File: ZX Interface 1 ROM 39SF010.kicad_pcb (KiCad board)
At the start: 2 copper layers, 24.5 x 32 mm, 14 parts, among them J2 Conn_01x09_Pin, J4 BBL-112-G-E, SW1 SW_SPDT, U1 SST39SF040A TSOP

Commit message: Add files via upload
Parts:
- renumbered J2 to J1
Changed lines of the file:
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@@
   (net 22 "/A9")
   (net 23 "/A8")
-  (net 24 "Net-(J2-Pin_1)")
-  (net 25 "Net-(J2-Pin_2)")
-  (net 26 "Net-(J2-Pin_3)")
-  (net 27 "Net-(J2-Pin_4)")
-  (net 28 "Net-(J2-Pin_5)")
-  (net 29 "Net-(J2-Pin_6)")
-  (net 30 "Net-(J2-Pin_7)")
-  (net 31 "Net-(J2-Pin_8)")
+  (net 24 "Net-(J1-Pin_1)")
+  (net 25 "Net-(J1-Pin_2)")
+  (net 26 "Net-(J1-Pin_3)")
+  (net 27 "Net-(J1-Pin_4)")
+  (net 28 "Net-(J1-Pin_5)")
+  (net 29 "Net-(J1-Pin_6)")
+  (net 30 "Net-(J1-Pin_7)")
+  (net 31 "Net-(J1-Pin_8)")
   (net 32 "Net-(R2-Pad2)")
   (net 33 "/A4")
@@
       (net 23 "/A8") (pinfunction "A8") (pintype "input"))
     (pad "4" smd roundrect locked (at -6.6875 -2.25 270) (size 1.575 0.3) (layers "F.Cu" "F.Paste" "F.Mask") (roundrect_rratio 0.25)
-      (net 30 "Net-(J2-Pin_7)") (pinfunction "A13") (pintype "input"))
+      (net 30 "Net-(J1-Pin_7)") (pinfunction "A13") (pintype "input"))
     (pad "5" smd roundrect locked (at -6.6875 -1.75 270) (size 1.575 0.3) (layers "F.Cu" "F.Paste" "F.Mask") (roundrect_rratio 0.25)
-      (net 29 "Net-(J2-Pin_6)") (pinfunction "A14") (pintype "input"))
+      (net 29 "Net-(J1-Pin_6)") (pinfunction "A14") (pintype "input"))
     (pad "6" smd roundrect locked (at -6.6875 -1.25 270) (size 1.575 0.3) (layers "F.Cu" "F.Paste" "F.Mask") (roundrect_rratio 0.25)
-      (net 26 "Net-(J2-Pin_3)") (pinfunction "A17") (pintype "input"))
+      (net 26 "Net-(J1-Pin_3)") (pinfunction "A17") (pintype "input"))
     (pad "7" smd roundrect locked (at -6.6875 -0.75 270) (size 1.575 0.3) (layers "F.Cu" "F.Paste" "F.Mask") (roundrect_rratio 0.25)
-      (net 24 "Net-(J2-Pin_1)") (pinfunction "WE") (pintype "input"))
+      (net 24 "Net-(J1-Pin_1)") (pinfunction "WE") (pintype "input"))
     (pad "8" smd roundrect locked (at -6.6875 -0.25 270) (size 1.575 0.3) (layers "F.Cu" "F.Paste" "F.Mask") (roundrect_rratio 0.25)
       (net 1 "/VCC") (pinfunction "VCC") (pintype "power_in"))
     (pad "9" smd roundrect locked (at -6.6875 0.25 270) (size 1.575 0.3) (layers "F.Cu" "F.Paste" "F.Mask") (roundrect_rratio 0.25)
-      (net 25 "Net-(J2-Pin_2)") (pinfunction "A18") (pintype "input"))
+      (net 25 "Net-(J1-Pin_2)") (pinfunction "A18") (pintype "input"))
     (pad "10" smd roundrect locked (at -6.6875 0.75 270) (size 1.575 0.3) (layers "F.Cu" "F.Paste" "F.Mask") (roundrect_rratio 0.25)
-      (net 27 "Net-(J2-Pin_4)") (pinfunction "A16") (pintype "input"))
+      (net 27 "Net-(J1-Pin_4)") (pinfunction "A16") (pintype "input"))
     (pad "11" smd roundrect locked (at -6.6875 1.25 270) (size 1.575 0.3) (layers "F.Cu" "F.Paste" "F.Mask") (roundrect_rratio 0.25)
-      (net 28 "Net-(J2-Pin_5)") (pinfunction "A15") (pintype "input"))
+      (net 28 "Net-(J1-Pin_5)") (pinfunction "A15") (pintype "input"))
     (pad "12" smd roundrect locked (at -6.6875 1.75 270) (size 1.575 0.3) (layers "F.Cu" "F.Paste" "F.Mask") (roundrect_rratio 0.25)
       (net 21 "/A12") (pinfunction "A12") (pintype "input"))
@@
       (net 17 "/D7") (pinfunction "DQ7") (pintype "tri_state"))
     (pad "30" smd roundrect locked (at 6.6875 -2.75 270) (size 1.575 0.3) (layers "F.Cu" "F.Paste" "F.Mask") (roundrect_rratio 0.25)
-      (net 31 "Net-(J2-Pin_8)") (pinfunction "CE") (pintype "input"))
+      (net 31 "Net-(J1-Pin_8)") (pinfunction "CE") (pintype "input"))
     (pad "31" smd roundrect locked (at 6.6875 -3.25 270) (size 1.575 0.3) (layers "F.Cu" "F.Paste" "F.Mask") (roundrect_rratio 0.25)
       (net 19 "/A10") (pinfunction "A10") (pintype "input"))
@@
     (property "ki_keywords" "connector")
     (attr through_hole)
-    (fp_text reference "J2" (at 0 -2.77) (layer "F.SilkS")
+    (fp_text reference "J1" (at 0 -2.77) (layer "F.SilkS")
         (effects (font (size 1 1) (thickness 0.15)))
     )
@@
       (stroke (width 0.1) (type solid)) (layer "F.Fab"))
     (pad "1" thru_hole rect locked (at 0 0) (size 1.7 1.7) (drill 1) (layers "*.Cu" "*.Mask")
-      (net 24 "Net-(J2-Pin_1)") (pinfunction "Pin_1") (pintype "passive"))
+      (net 24 "Net-(J1-Pin_1)") (pinfunction "Pin_1") (pintype "passive"))
     (pad "2" thru_hole oval locked (at 0 2.54) (size 1.7 1.7) (drill 1) (layers "*.Cu" "*.Mask")
-      (net 25 "Net-(J2-Pin_2)") (pinfunction "Pin_2") (pintype "passive"))
+      (net 25 "Net-(J1-Pin_2)") (pinfunction "Pin_2") (pintype "passive"))
     (pad "3" thru_hole oval locked (at 0 5.08) (size 1.7 1.7) (drill 1) (layers "*.Cu" "*.Mask")
-      (net 26 "Net-(J2-Pin_3)") (pinfunction "Pin_3") (pintype "passive"))
+      (net 26 "Net-(J1-Pin_3)") (pinfunction "Pin_3") (pintype "passive"))
     (pad "4" thru_hole oval locked (at 0 7.62) (size 1.7 1.7) (drill 1) (layers "*.Cu" "*.Mask")
-      (net 27 "Net-(J2-Pin_4)") (pinfunction "Pin_4") (pintype "passive"))
+      (net 27 "Net-(J1-Pin_4)") (pinfunction "Pin_4") (pintype "passive"))
     (pad "5" thru_hole oval locked (at 0 10.16) (size 1.7 1.7) (drill 1) (layers "*.Cu" "*.Mask")
-      (net 28 "Net-(J2-Pin_5)") (pinfunction "Pin_5") (pintype "passive"))
+      (net 28 "Net-(J1-Pin_5)") (pinfunction "Pin_5") (pintype "passive"))
     (pad "6" thru_hole oval locked (at 0 12.7) (size 1.7 1.7) (drill 1) (layers "*.Cu" "*.Mask")
-      (net 29 "Net-(J2-Pin_6)") (pinfunction "Pin_6") (pintype "passive"))
+      (net 29 "Net-(J1-Pin_6)") (pinfunction "Pin_6") (pintype "passive"))
     (pad "7" thru_hole oval locked (at 0 15.24) (size 1.7 1.7) (drill 1) (layers "*.Cu" "*.Mask")
-      (net 30 "Net-(J2-Pin_7)") (pinfunction "Pin_7") (pintype "passive"))
+      (net 30 "Net-(J1-Pin_7)") (pinfunction "Pin_7") (pintype "passive"))
     (pad "8" thru_hole oval locked (at 0 17.78) (size 1.7 1.7) (drill 1) (layers "*.Cu" "*.Mask")
-      (net 31 "Net-(J2-Pin_8)") (pinfunction "Pin_8") (pintype "passive"))
+      (net 31 "Net-(J1-Pin_8)") (pinfunction "Pin_8") (pintype "passive"))
     (pad "9" thru_hole oval locked (at 0 20.32) (size 1.7 1.7) (drill 1) (layers "*.Cu" "*.Mask")
       (net 2 "GND") (pinfunction "Pin_9") (pintype "passive"))
@@
       (stroke (width 0.1) (type solid)) (layer "B.Fab"))
     (pad "1" smd roundrect locked (at -1.55 0 180) (size 1.3 1.75) (layers "B.Cu" "B.Paste" "B.Mask") (roundrect_rratio 0.1923076923)
-      (net 28 "Net-(J2-Pin_5)") (pintype "passive"))
+      (net 28 "Net-(J1-Pin_5)") (pintype "passive"))
     (pad "2" smd roundrect locked (at 1.55 0 180) (size 1.3 1.75) (layers "B.Cu" "B.Paste" "B.Mask") (roundrect_rratio 0.1923076923)
       (net 1 "/VCC") (pintype "passive"))
@@
       (stroke (width 0.1) (type solid)) (layer "B.Fab"))
     (pad "1" smd roundrect locked (at -1.55 0 180) (size 1.3 1.75) (layers "B.Cu" "B.Paste" "B.Mask") (roundrect_rratio 0.1923076923)
-      (net 31 "Net-(J2-Pin_8)") (pintype "passive"))
+      (net 31 "Net-(J1-Pin_8)") (pintype "passive"))
     (pad "2" smd roundrect locked (at 1.55 0 180) (size 1.3 1.75) (layers "B.Cu" "B.Paste" "B.Mask") (roundrect_rratio 0.1923076923)
       (net 2 "GND") (pintype "passive"))
@@
       (stroke (width 0.1) (type solid)) (layer "B.Fab"))
     (pad "1" smd roundrect locked (at -1.55 0 180) (size 1.3 1.75) (layers "B.Cu" "B.Paste" "B.Mask") (roundrect_rratio 0.1923076923)
-      (net 27 "Net-(J2-Pin_4)") (pintype "passive"))
+      (net 27 "Net-(J1-Pin_4)") (pintype "passive"))
     (pad "2" smd roundrect locked (at 1.55 0 180) (size 1.3 1.75) (layers "B.Cu" "B.Paste" "B.Mask") (roundrect_rratio 0.1923076923)
       (net 32 "Net-(R2-Pad2)") (pintype "passive"))
@@
       (stroke (width 0.1) (type solid)) (layer "B.Fab"))
     (pad "1" smd roundrect locked (at -1.55 0 180) (size 1.3 1.75) (layers "B.Cu" "B.Paste" "B.Mask") (roundrect_rratio 0.1923076923)
-      (net 30 "Net-(J2-Pin_7)") (pintype "passive"))
+      (net 30 "Net-(J1-Pin_7)") (pintype "passive"))
     (pad "2" smd roundrect locked (at 1.55 0 180) (size 1.3 1.75) (layers "B.Cu" "B.Paste" "B.Mask") (roundrect_rratio 0.1923076923)
       (net 1 "/VCC") (pintype "passive"))
@@
       (stroke (width 0.1) (type solid)) (layer "B.Fab"))
     (pad "1" smd roundrect locked (at -1.55 0 180) (size 1.3 1.75) (layers "B.Cu" "B.Paste" "B.Mask") (roundrect_rratio 0.1923076923)
-      (net 26 "Net-(J2-Pin_3)") (pintype "passive"))
+      (net 26 "Net-(J1-Pin_3)") (pintype "passive"))
     (pad "2" smd roundrect locked (at 1.55 0 180) (size 1.3 1.75) (layers "B.Cu" "B.Paste" "B.Mask") (roundrect_rratio 0.1923076923)
       (net 1 "/VCC") (pintype "passive"))
@@
       (net 1 "/VCC") (pintype "passive"))
     (pad "2" smd roundrect locked (at 1.55 0 270) (size 1.3 1.75) (layers "B.Cu" "B.Paste" "B.Mask") (roundrect_rratio 0.1923076923)
-      (net 24 "Net-(J2-Pin_1)") (pintype "passive"))
+      (net 24 "Net-(J1-Pin_1)") (pintype "passive"))
     (model "${KICAD6_3DMODEL_DIR}/Resistor_SMD.3dshapes/R_1206_3216Metric.wrl"
       (offset (xyz 0 0 0))
@@
       (stroke (width 0.1) (type solid)) (layer "B.Fab"))
     (pad "1" smd roundrect locked (at -1.55 0 180) (size 1.3 1.75) (layers "B.Cu" "B.Paste" "B.Mask") (roundrect_rratio 0.1923076923)
-      (net 25 "Net-(J2-Pin_2)") (pintype "passive"))
+      (net 25 "Net-(J1-Pin_2)") (pintype "passive"))
     (pad "2" smd roundrect locked (at 1.55 0 180) (size 1.3 1.75) (layers "B.Cu" "B.Paste" "B.Mask") (roundrect_rratio 0.1923076923)
       (net 1 "/VCC") (pintype "passive"))
@@
       (stroke (width 0.1) (type solid)) (layer "B.Fab"))
     (pad "1" smd roundrect locked (at -1.55 0 180) (size 1.3 1.75) (layers "B.Cu" "B.Paste" "B.Mask") (roundrect_rratio 0.1923076923)
-      (net 29 "Net-(J2-Pin_6)") (pintype "passive"))
+      (net 29 "Net-(J1-Pin_6)") (pintype "passive"))
     (pad "2" smd roundrect locked (at 1.55 0 180) (size 1.3 1.75) (layers "B.Cu" "B.Paste" "B.Mask") (roundrect_rratio 0.1923076923)
       (net 1 "/VCC") (pintype "passive"))

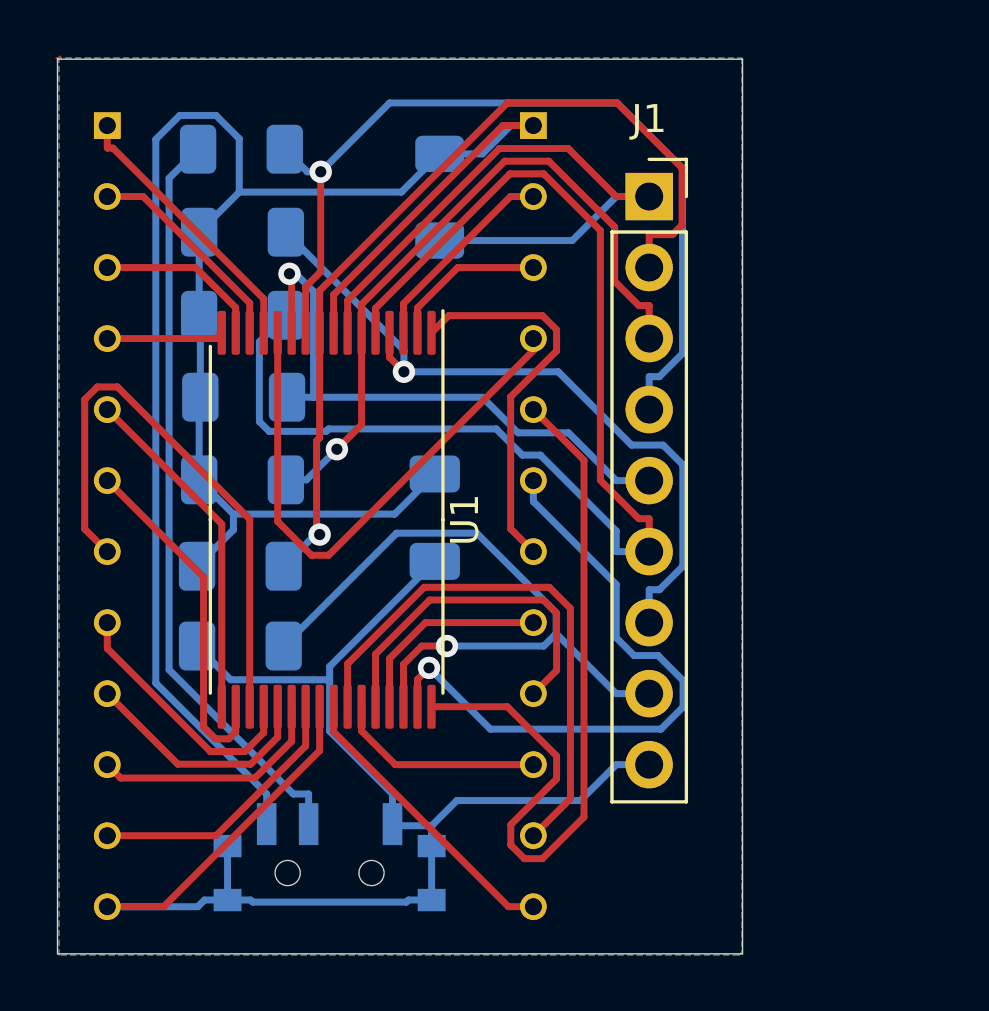
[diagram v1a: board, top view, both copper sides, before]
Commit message: Updated to use Right Angle 9 pin Header
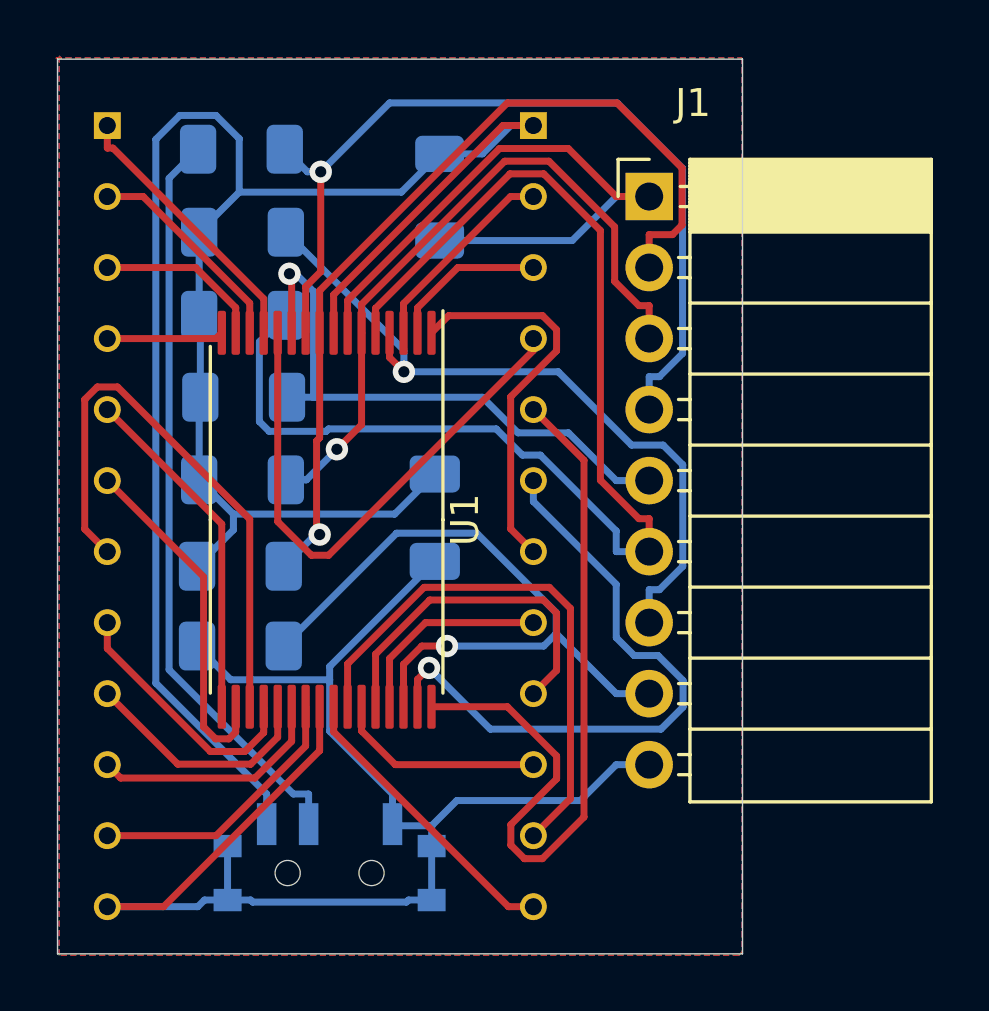
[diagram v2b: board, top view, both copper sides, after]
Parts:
- J1: footprint Connector_PinSocket_2.54mm:PinSocket_1x09_P2.54mm_Vertical -> Switch:PinSocket_1x09_P2.54mm_HorizontalR
- moved J1 10.2 mm to (180.3, 107.4)

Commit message: Add files via upload
Updated file to Kicad 9. Restructured folders. Added ibom (Interactive BOM)
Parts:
- C1: footprint Capacitor_SMD:C_1206_3216Metric_Pad1.33x1.80mm_HandSolder -> Mod:C_1206_3216Metric_Pad1.33x1.80mm_HandSolder
- J1: footprint Switch:PinSocket_1x09_P2.54mm_HorizontalR -> Mod:PinSocket_1x09_P2.54mm_HorizontalR
- J3: renamed from locked; footprint Switch:Pin-Pin Header 2.54mm Round Samtec BBL-112-G-E -> Mod:Pin-Pin Header 2.54mm Round Samtec BBL-112-G-E
- J4: footprint Switch:Pin-Pin Header 2.54mm Round Samtec BBL-112-G-E -> Mod:Pin-Pin Header 2.54mm Round Samtec BBL-112-G-E
- R1, R2, R3, R4, R5, R6, R7, R8: footprint Resistor_SMD:R_1206_3216Metric_Pad1.30x1.75mm_HandSolder -> Mod:R_1206_3216Metric_Pad1.30x1.75mm_HandSolder
- SW1: footprint Switch:SW_PCM12SMTR -> Mod:SW_PCM12SMTR
- U1: footprint Package_SO:TSOP-I-32_12.4x8mm_P0.5mm -> Mod:TSOP-I-32_12.4x8mm_P0.5mm
